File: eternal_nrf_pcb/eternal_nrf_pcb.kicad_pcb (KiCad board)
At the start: 4 copper layers, 27.5 x 42.5 mm, 55 parts, among them J1 Conn_01x07_Pin, Q1 IRLML6244, Q2 IRLML6402, SW1 SW_Push, U1 BQ25504, U2 nRF52810-QCxx, U3 DRV5032DU, U4 SHTC3, Y1 Crystal_GND24, Y2 Crystal

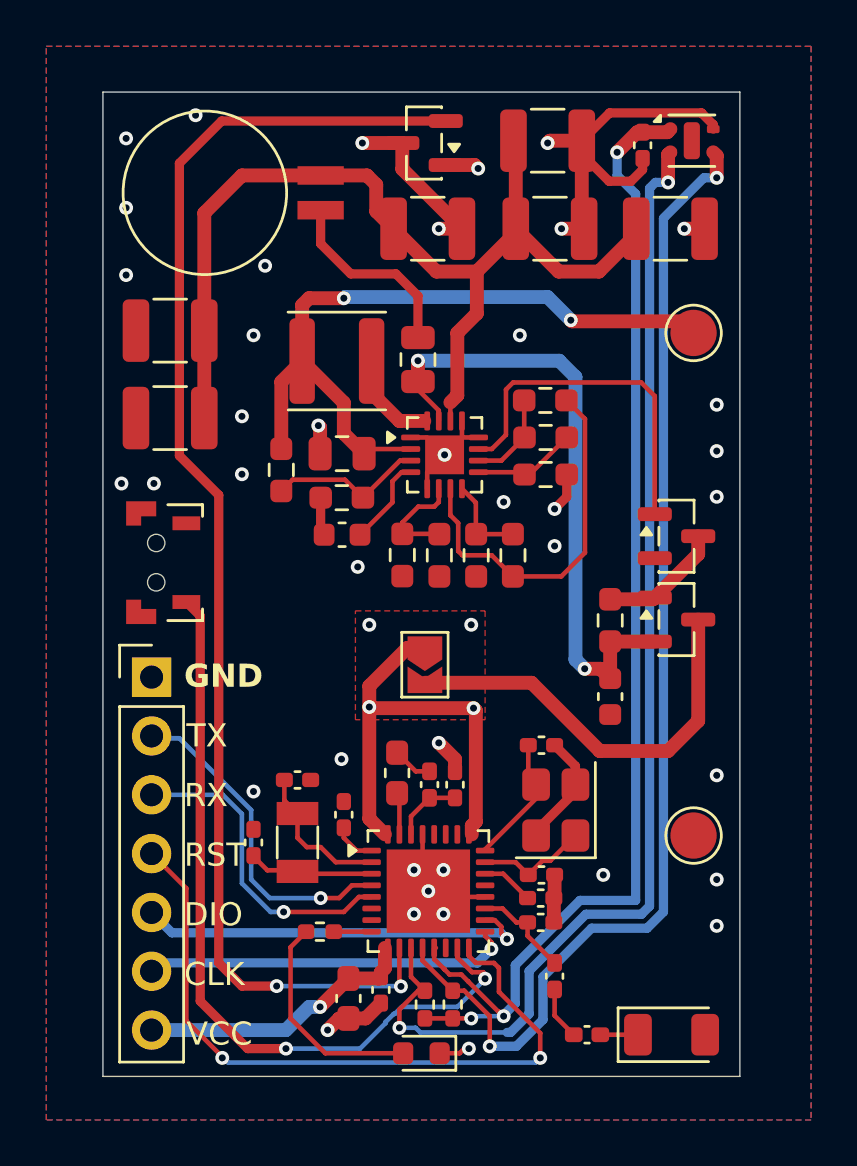
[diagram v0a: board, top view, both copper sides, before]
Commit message: increase trace width
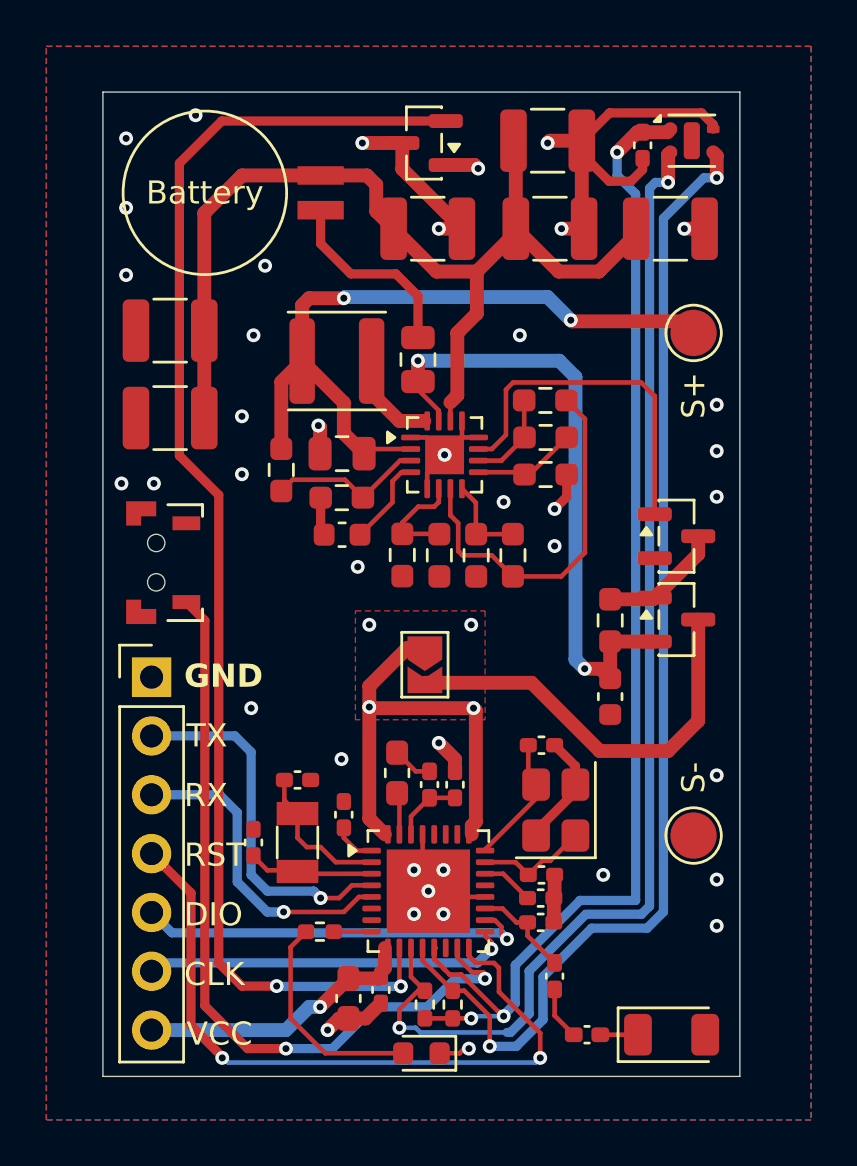
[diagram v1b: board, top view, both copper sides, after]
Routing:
- net TX: track 14.5 -> 15.8 mm

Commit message: add production file
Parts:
- added C22: 100nF, Capacitor_SMD:C_0402_1005Metric_Pad0.74x0.62mm_HandSolder, F.Cu at (142.2, 105.0)
- U3: value DRV5032DU -> DRV5032
- moved C9 11.8 mm to (135.2, 102.3), turned to 90 degrees
- moved C20 0.10 mm to (131.6, 107.4)
- moved C21 0.10 mm to (133.4, 104.8)
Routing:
- net VCC: track 35.7 -> 33.8 mm
- net GND: track 60.2 -> 62.0 mm, vias 39 -> 41

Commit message: fix bugs
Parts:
- R3, R5: value 4.32M -> 4.02M
- R4: value 6.34M -> 5.90M
- R6: value 5.62M -> 5.90M
- R7: value 1.43M -> 2.26M
- R8: value 4.12M -> 3.32M
- U3: value DRV5032 -> DRV5032DU
- moved R9 3.20 mm to (144.1, 88.3)
- moved R8 1.58 mm to (144.1, 91.5)
- moved R7 1.58 mm to (144.1, 89.9)
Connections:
- R7 pad 2: Net-(U1-OK_PROG) -> Net-(U1-OK_HYST)
- R8 pad 1: Net-(U1-OK_PROG) -> Net-(U1-OK_HYST)
- R8 pad 2: Net-(U1-OK_HYST) -> Net-(U1-OK_PROG)
- R9 pad 1: Net-(U1-OK_HYST) -> Net-(U1-OK_PROG)
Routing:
- net Net-(U1-OK_PROG): track 4.01 -> 7.72 mm
- net GND: track 62.0 -> 60.3 mm
- net Net-(U1-VRDIV): track 16.1 -> 14.5 mm
- net Net-(U1-OK_HYST): track 4.52 -> 3.98 mm
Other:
- board text added: "Rev. 1, 10th May 2026 Madhukar Temba"
- board text removed: "Rev. 1, 9th May 2026 Madhukar Temba"

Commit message: final production file
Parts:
- L5: value 6.8uH -> 6.8nH
- R13: value 4.7K -> 1K
- SW1: value SW_Push -> TSA002A3216A
- U2: value nRF52810-QCxx -> nRF52810-QCAA
- Y1: value Crystal_GND24 -> S3232000081040
- Y2: value Crystal -> X1A0001410003
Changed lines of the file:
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@@
 			)
 		)
-		(property "Value" "6.8uH"
+		(property "Value" "6.8nH"
 			(at 0 1.17 0)
 			(layer "User.3")
@@
 			)
 		)
-		(property "Value" "Crystal"
+		(property "Value" "X1A0001410003"
 			(at 0 2 90)
 			(layer "User.3")
@@
 			)
 		)
-		(property "Value" "Crystal_GND24"
+		(property "Value" "S3232000081040"
 			(at 0 2.45 90)
 			(layer "User.3")
@@
 			)
 		)
-		(property "Value" "nRF52810-QCxx"
+		(property "Value" "nRF52810-QCAA"
 			(at 0 3.8 0)
 			(layer "User.3")
@@
 			)
 		)
-		(property "Value" "4.7K"
+		(property "Value" "1K"
 			(at -0.2 -1.4 0)
 			(layer "User.3")
@@
 			)
 		)
-		(property "Value" "SW_Push"
+		(property "Value" "TSA002A3216A"
 			(at -4.2 -0.9 90)
 			(layer "User.3")
@@
 	)
 	(segment
-		(start 144.5 114.8725)
+		(start 145.085787 115.458287)
 		(end 145.3275 115.7)
 		(width 0.2)
@@
 	(segment
 		(start 144.5 113.745)
-		(end 144.5 114.8725)
+		(end 144.5 114.044073)
+		(width 0.2)
+		(layer "F.Cu")
+		(net "Net-(L2-Pad1)")
+	)
+	(arc
+		(start 145.085787 115.458287)
+		(mid 144.652241 114.80944)
+		(end 144.5 114.044073)
 		(width 0.2)
 		(layer "F.Cu")
@@
 	)
 	(segment
-		(start 143.2 91.5125)
-		(end 143.425 91.5125)
+		(start 142.4 90.365686)
+		(end 141.853186 90.9125)
 		(width 0.2)
 		(layer "F.Cu")
-		(net "Net-(U1-OK_HYST)")
+		(net "Net-(U1-OK_PROG)")
 	)
 	(segment
-		(start 143.1875 89.9)
-		(end 143.2 89.9125)
+		(start 144.1 89.2125)
+		(end 143.2 88.3125)
 		(width 0.2)
 		(layer "F.Cu")
-		(net "Net-(U1-OK_HYST)")
+		(net "Net-(U1-OK_PROG)")
 	)
 	(segment
-		(start 143.1875 89.8875)
-		(end 143.1875 91.475)
+		(start 142.4 89.1125)
+		(end 142.4 90.365686)
 		(width 0.2)
 		(layer "F.Cu")
-		(net "Net-(U1-OK_HYST)")
+		(net "Net-(U1-OK_PROG)")
 	)
 	(segment
-		(start 143.1875 91.475)
-		(end 143.175 91.4875)
+		(start 145 91.4875)
+		(end 144.1 90.5875)
 		(width 0.2)
 		(layer "F.Cu")
-		(net "Net-(U1-OK_HYST)")
+		(net "Net-(U1-OK_PROG)")
 	)
 	(segment
-		(start 143.175 91.4875)
-		(end 141.2875 91.4875)
+		(start 144.1 90.5875)
+		(end 144.1 89.2125)
 		(width 0.2)
 		(layer "F.Cu")
-		(net "Net-(U1-OK_HYST)")
+		(net "Net-(U1-OK_PROG)")
 	)
 	(segment
-		(start 143.1 91.4125)
-		(end 143.2 91.5125)
+		(start 143.2 88.3125)
+		(end 142.4 89.1125)
 		(width 0.2)
 		(layer "F.Cu")
-		(net "Net-(U1-OK_HYST)")
+		(net "Net-(U1-OK_PROG)")
 	)
 	(segment
-		(start 141.2875 91.4875)
-		(end 141.2125 91.4125)
+		(start 141.853186 90.9125)
+		(end 141.2125 90.9125)
 		(width 0.2)
 		(layer "F.Cu")
-		(net "Net-(U1-OK_HYST)")
+		(net "Net-(U1-OK_PROG)")
 	)
 	(segment
@@
 	)
 	(via
-		(at 131.3 95.9)
+		(at 131.2 95.4)
 		(size 0.6)
 		(drill 0.3)
@@
 	)
 	(via
-		(at 131.5 85.5)
+		(at 131.2 85.65)
 		(size 0.6)
 		(drill 0.3)
@@
 	)
 	(via
-		(at 131 89)
+		(at 131.2 88.9)
 		(size 0.6)
 		(drill 0.3)
@@
 	)
 	(via
-		(at 131.3 101.9)
+		(at 131.2 101.9)
 		(size 0.6)
 		(drill 0.3)
@@
 	)
 	(via
-		(at 131.3 98.8)
+		(at 131.2 98.65)
 		(size 0.6)
 		(drill 0.3)
@@
 	)
 	(via
-		(at 132 82.5)
+		(at 131.2 82.4)
 		(size 0.6)
 		(drill 0.3)
@@
 	)
 	(via
-		(at 131 91.5)
+		(at 131.2 92.15)
 		(size 0.6)
 		(drill 0.3)
@@
 	)
 	(segment
-		(start 142.4 90.365686)
-		(end 141.853186 90.9125)
+		(start 143.2 91.5125)
+		(end 143.425 91.5125)
 		(width 0.2)
 		(layer "F.Cu")
-		(net "Net-(U1-OK_PROG)")
+		(net "Net-(U1-OK_HYST)")
 	)
 	(segment
-		(start 144.1 89.2125)
-		(end 143.2 88.3125)
+		(start 143.1875 89.9)
+		(end 143.2 89.9125)
 		(width 0.2)
 		(layer "F.Cu")
-		(net "Net-(U1-OK_PROG)")
+		(net "Net-(U1-OK_HYST)")
 	)
 	(segment
-		(start 142.4 89.1125)
-		(end 142.4 90.365686)
+		(start 143.1875 89.8875)
+		(end 143.1875 91.475)
 		(width 0.2)
 		(layer "F.Cu")
-		(net "Net-(U1-OK_PROG)")
+		(net "Net-(U1-OK_HYST)")
 	)
 	(segment
-		(start 145 91.4875)
-		(end 144.1 90.5875)
+		(start 143.1875 91.475)
+		(end 143.175 91.4875)
 		(width 0.2)
 		(layer "F.Cu")
-		(net "Net-(U1-OK_PROG)")
+		(net "Net-(U1-OK_HYST)")
 	)
 	(segment
-		(start 144.1 90.5875)
-		(end 144.1 89.2125)
+		(start 143.175 91.4875)
+		(end 141.2875 91.4875)
 		(width 0.2)
 		(layer "F.Cu")
-		(net "Net-(U1-OK_PROG)")
+		(net "Net-(U1-OK_HYST)")
 	)
 	(segment
-		(start 143.2 88.3125)
-		(end 142.4 89.1125)
+		(start 143.1 91.4125)
+		(end 143.2 91.5125)
 		(width 0.2)
 		(layer "F.Cu")
-		(net "Net-(U1-OK_PROG)")
+		(net "Net-(U1-OK_HYST)")
 	)
 	(segment
-		(start 141.853186 90.9125)
-		(end 141.2125 90.9125)
+		(start 141.2875 91.4875)
+		(end 141.2125 91.4125)
 		(width 0.2)
 		(layer "F.Cu")
-		(net "Net-(U1-OK_PROG)")
+		(net "Net-(U1-OK_HYST)")
 	)
 	(segment
@@
 	)
 	(segment
-		(start 143.3325 111.4325)
+		(start 143.625393 111.725393)
 		(end 144.5 112.6)
 		(width 0.2)
@@
 	(segment
 		(start 141.5 110.25)
-		(end 142.25 110.25)
+		(end 141.835786 110.25)
 		(width 0.2)
 		(layer "F.Cu")
@@
 	)
 	(segment
-		(start 142.85 110.85)
+		(start 143.264214 110.85)
 		(end 143.3325 110.85)
 		(width 0.2)
@@
 	(segment
 		(start 143.3325 110.85)
-		(end 143.3325 111.4325)
+		(end 143.3325 111.018286)
 		(width 0.2)
 		(layer "F.Cu")
@@
 	)
 	(segment
-		(start 142.25 110.25)
-		(end 142.85 110.85)
+		(start 142.542893 110.542893)
+		(end 142.557107 110.557107)
+		(width 0.2)
+		(layer "F.Cu")
+		(net "Net-(U2-ANT)")
+	)
+	(arc
+		(start 143.264214 110.85)
+		(mid 142.881531 110.77388)
+		(end 142.557107 110.557107)
+		(width 0.2)
+		(layer "F.Cu")
+		(net "Net-(U2-ANT)")
+	)
+	(arc
+		(start 141.835786 110.25)
+		(mid 142.218469 110.32612)
+		(end 142.542893 110.542893)
+		(width 0.2)
+		(layer "F.Cu")
+		(net "Net-(U2-ANT)")
+	)
+	(arc
+		(start 143.625393 111.725393)
+		(mid 143.40862 111.40097)
+		(end 143.3325 111.018286)
 		(width 0.2)
 		(layer "F.Cu")

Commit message: add missing route :(
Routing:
- net Net-(U1-VRDIV): track 14.5 -> 17.7 mm
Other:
- board text added: "Rev. 2, 20th May 2026 Madhukar Temba"
- board text removed: "Rev. 1, 10th May 2026 Madhukar Temba"
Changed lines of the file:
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@@
 	(title_block
 		(title "Eternal nRF")
-		(date "2026-05-10")
-		(rev "1")
+		(date "2026-05-20")
+		(rev "2")
 		(company "Madhukar Temba")
 	)
@@
 		)
 	)
-	(gr_text "Rev. 1, 10th May 2026\nMadhukar Temba"
+	(gr_text "Rev. 2, 20th May 2026\nMadhukar Temba"
 		(at 149.425 78.1 90)
 		(layer "B.SilkS")
@@
 			(justify left bottom mirror)
 		)
-		(render_cache "Rev. 1, 10th May 2026\nMadhukar Temba" 90
+		(render_cache "Rev. 2, 20th May 2026\nMadhukar Temba" 90
 			(polygon
 				(pts
@@
 			(polygon
 				(pts
-					(xy 147.205 82.412254) (xy 146.333639 82.412254) (xy 146.504877 82.190676) (xy 146.305136 82.04457)
-					(xy 146.018565 82.435774) (xy 146.018565 82.694281) (xy 147.205 82.694281)
+					(xy 147.205 82.051311) (xy 146.971186 82.051311) (xy 146.553604 82.514689) (xy 146.510524 82.554862)
+					(xy 146.468461 82.585177) (xy 146.422785 82.605272) (xy 146.371594 82.612069) (xy 146.330946 82.607345)
+					(xy 146.297227 82.593886) (xy 146.268866 82.571769) (xy 146.247485 82.542732) (xy 146.234277 82.507485)
+					(xy 146.229591 82.464277) (xy 146.235278 82.419494) (xy 146.251679 82.381736) (xy 146.279124 82.349312)
+					(xy 146.314418 82.324311) (xy 146.357246 82.306542) (xy 146.409256 82.296409) (xy 146.372327 82.026106)
+					(xy 146.285411 82.043892) (xy 146.210467 82.075638) (xy 146.144206 82.120567) (xy 146.088907 82.175509)
+					(xy 146.044773 82.239969) (xy 146.012191 82.313995) (xy 145.992444 82.393836) (xy 145.985739 82.479445)
+					(xy 145.99123 82.560641) (xy 146.007575 82.638886) (xy 146.035536 82.712424) (xy 146.074766 82.776566)
+					(xy 146.125746 82.830746) (xy 146.188925 82.873066) (xy 146.236052 82.892706) (xy 146.289376 82.904924)
+					(xy 146.350052 82.90919) (xy 146.411944 82.904815) (xy 146.46509 82.892411) (xy 146.514494 82.872418)
+					(xy 146.559905 82.846249) (xy 146.602034 82.814823) (xy 146.641385 82.779057) (xy 146.71605 82.701022)
+					(xy 146.961147 82.425662) (xy 146.961147 82.910875) (xy 147.205 82.910875)
 				)
 			)
@@
 			(polygon
 				(pts
-					(xy 147.205 84.368932) (xy 146.333639 84.368932) (xy 146.504877 84.147355) (xy 146.305136 84.001249)
-					(xy 146.018565 84.392452) (xy 146.018565 84.650959) (xy 147.205 84.650959)
+					(xy 147.205 84.00799) (xy 146.971186 84.00799) (xy 146.553604 84.471367) (xy 146.510524 84.511541)
+					(xy 146.468461 84.541856) (xy 146.422785 84.56195) (xy 146.371594 84.568747) (xy 146.330946 84.564023)
+					(xy 146.297227 84.550564) (xy 146.268866 84.528447) (xy 146.247485 84.49941) (xy 146.234277 84.464164)
+					(xy 146.229591 84.420956) (xy 146.235278 84.376172) (xy 146.251679 84.338415) (xy 146.279124 84.30599)
+					(xy 146.314418 84.280989) (xy 146.357246 84.263221) (xy 146.409256 84.253087) (xy 146.372327 83.982784)
+					(xy 146.285411 84.000571) (xy 146.210467 84.032316) (xy 146.144206 84.077245) (xy 146.088907 84.132187)
+					(xy 146.044773 84.196647) (xy 146.012191 84.270673) (xy 145.992444 84.350515) (xy 145.985739 84.436123)
+					(xy 145.99123 84.51732) (xy 146.007575 84.595565) (xy 146.035536 84.669102) (xy 146.074766 84.733244)
+					(xy 146.125746 84.787425) (xy 146.188925 84.829745) (xy 146.236052 84.849384) (xy 146.289376 84.861602)
+					(xy 146.350052 84.865868) (xy 146.411944 84.861493) (xy 146.46509 84.849089) (xy 146.514494 84.829097)
+					(xy 146.559905 84.802927) (xy 146.602034 84.771501) (xy 146.641385 84.735736) (xy 146.71605 84.6577)
+					(xy 146.961147 84.382341) (xy 146.961147 84.867554) (xy 147.205 84.867554)
 				)
 			)
@@
 	)
 	(segment
+		(start 140.1 95)
+		(end 140.4 95)
+		(width 0.2)
+		(locked yes)
+		(layer "F.Cu")
+		(net "Net-(U1-VRDIV)")
+	)
+	(segment
+		(start 138.3 95)
+		(end 140.1 95)
+		(width 0.2)
+		(layer "F.Cu")
+		(net "Net-(U1-VRDIV)")
+	)
+	(segment
 		(start 140.520778 95)
 		(end 141.7875 95)
@@
 	)
 	(segment
+		(start 137.925 95.375)
+		(end 138.3 95)
+		(width 0.2)
+		(layer "F.Cu")
+		(net "Net-(U1-VRDIV)")
+	)
+	(segment
+		(start 140.3375 93.608278)
+		(end 140.3375 94.9375)
+		(width 0.2)
+		(layer "F.Cu")
+		(net "Net-(U1-VRDIV)")
+	)
+	(segment
 		(start 145.8125 90.6875)
 		(end 145.0125 89.8875)
@@
 	)
 	(segment
-		(start 140.3375 93.608278)
-		(end 140.3375 94.816722)
+		(start 140.3375 94.9375)
+		(end 140.4 95)
+		(width 0.2)
+		(layer "F.Cu")
+		(net "Net-(U1-VRDIV)")
+	)
+	(segment
+		(start 137.925 95.9)
+		(end 137.925 95.375)
 		(width 0.2)
 		(layer "F.Cu")
@@
 	)
 	(segment
+		(start 140.4 95)
+		(end 140.520778 95)
+		(width 0.2)
+		(locked yes)
+		(layer "F.Cu")
+		(net "Net-(U1-VRDIV)")
+	)
+	(segment
 		(start 141.7875 95)
 		(end 142.7 95.9125)
@@
 		(width 0.2)
 		(layer "F.Cu")
-		(net "Net-(U1-VRDIV)")
-	)
-	(segment
-		(start 140.3375 94.816722)
-		(end 140.520778 95)
-		(width 0.2)
-		(layer "F.Cu")
